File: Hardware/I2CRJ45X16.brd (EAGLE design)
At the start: 146 x 50 mm, 91 parts, among them IC1 MCP23017SO, IC2 MCP23017SO, IC3 MCP23017SO, IC4 MCP23017SO, J1 I2C-BREAKOUT, J2 I2C-BREAKOUT, J3 M01-PLAIN, J4 RJ45-X8, J5 RJ45-X8

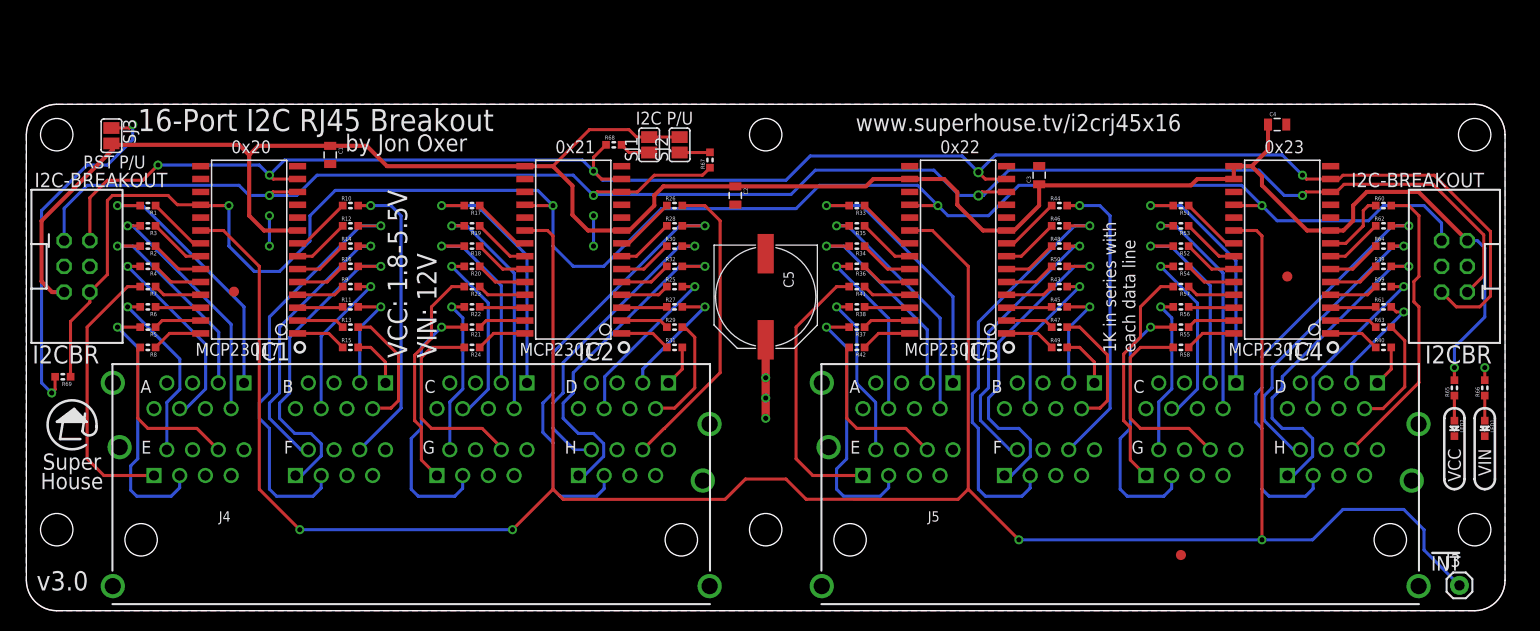
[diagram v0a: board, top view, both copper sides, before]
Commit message: Regenerated 16-port version from updated 24-port version.
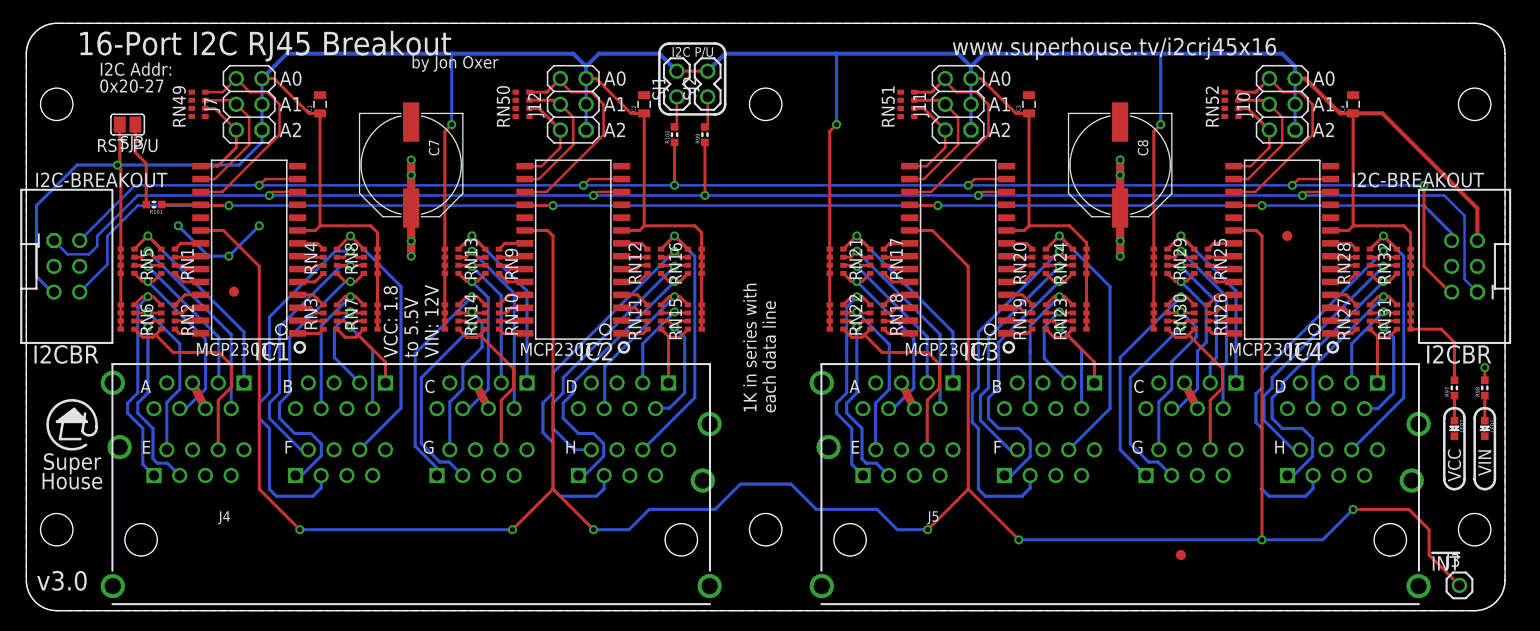
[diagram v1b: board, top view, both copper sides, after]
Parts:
- removed C5: 330uF 50V, SuperHouse-DiscreteSemi:PANASONIC_G
- removed R1, R10, R11, R12, R13, R14, R15, R16, R17, R18, R19, R2, R20, R21, R22, R23, R24, R25, R26, R27, R28, R29, R3, R30, R31, R32, R33, R34, R35, R36, R37, R38, R39, R4, R40, R41, R42, R43, R44, R45, R46, R47, R48, R49, R5, R50, R51, R52, R53, R54, R55, R56, R57, R58, R59, R6, R60, R61, R62, R63, R64, R7, R8, R9: 1K, SuperHouse-DiscreteSemi:R0603
- removed R65, R66, R67, R68: 4K7, SuperHouse-DiscreteSemi:R0603
- removed R69: 10K, SuperHouse-DiscreteSemi:R0603
- added C7, C8: 330uF 50V, SuperHouse-Capacitors:PANASONIC_G
- added J10: I2C Addr 4, SuperHouse-Connectors:2X03-P
- added J11: I2C Addr 3, SuperHouse-Connectors:2X03-P
- added J12: I2C Addr 2, SuperHouse-Connectors:2X03-P
- added J7: I2C Addr 1, SuperHouse-Connectors:2X03-P
- added R100, R97, R98, R99: 4K7, SuperHouse-Resistors:R0603
- added R101: 10K, SuperHouse-Resistors:R0603
- added RN1, RN10, RN11, RN12, RN17, RN18, RN19, RN2, RN20, RN25, RN26, RN27, RN28, RN3, RN4, RN9: 1K, SuperHouse-Resistors:CAY16
- added RN13, RN14, RN15, RN16, RN21, RN22, RN23, RN24, RN29, RN30, RN31, RN32, RN49, RN5, RN50, RN51, RN52, RN6, RN7, RN8: 10K, SuperHouse-Resistors:CAY16
- C1, C2, C3, C4: device SuperHouse-DiscreteSemi:C0805 -> SuperHouse-Capacitors:C0805
- J1, J2: device SuperHouse-Connectors:2X03-SHROUDED -> SuperHouse-Connectors:2X3-2.54-SHROUDED
- SJ1, SJ2: device SuperHouse-Jumpers:SJ -> SuperHouse-Connectors:1X02-P
- moved C2 12.7 mm to (61.0, 50.0), turned to 90 degrees
- moved C4 7.76 mm to (131.0, 50.0), turned to 90 degrees
- moved C3 7.07 mm to (99.0, 50.0)
- moved SJ2 6.61 mm to (67.3, 52.0)
- moved SJ1 6.59 mm to (64.2, 52.0)
- moved C1 5.10 mm to (29.0, 50.0), turned to 90 degrees
- moved FID2 4.00 mm to (124.5, 37.0)
- moved SJ3 1.94 mm to (10.0, 48.0), turned to 180 degrees
- moved J1 1.00 mm to (4.00, 34.0), turned to 270 degrees
- moved J2 1.00 mm to (142.0, 34.0), turned to 90 degrees
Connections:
- new net N$10: IC2.16, J12.4, RN50.7
- new net N$11: IC2.17, J12.6, RN50.8
- new net N$12: IC3.17, J11.6, RN51.8
- new net N$13: IC3.15, J11.2, RN51.6
- new net N$14: IC3.16, J11.4, RN51.7
- new net N$15: IC4.17, J10.6, RN52.8
- new net N$16: IC4.15, J10.2, RN52.6
- new net N$17: IC4.16, J10.4, RN52.7
- new net N$4: IC1.17, J7.6, RN49.8
- new net N$5: IC1.16, J7.4, RN49.7
- new net N$6: IC1.15, J7.2, RN49.6
- new net N$9: IC2.15, J12.2, RN50.6
- net !RESET: now also R101.1; no longer R69.1
- net 1A1: now also RN1.5, RN5.4; no longer R1.2
- net 1A2: now also RN1.6, RN5.3; no longer R3.2
- net 1A3: now also RN1.7, RN5.2; no longer R2.2
- net 1A6: now also RN1.8, RN5.1; no longer R4.2
- net 1B1: now also RN3.5, RN7.4; no longer R15.2
- net 1B2: now also RN3.6, RN7.3; no longer R13.2
- net 1B3: now also RN3.7, RN7.2; no longer R11.2
- net 1B6: now also RN3.8, RN7.1; no longer R9.2
- net 1C1: now also RN13.4, RN9.5; no longer R17.2
- net 1C2: now also RN13.3, RN9.6; no longer R19.2
- net 1C3: now also RN13.2, RN9.7; no longer R18.2
- net 1C6: now also RN13.1, RN9.8; no longer R20.2
- net 1D1: now also RN11.5, RN15.4; no longer R31.2
- net 1D2: now also RN11.6, RN15.3; no longer R29.2
- net 1D3: now also RN11.7, RN15.2; no longer R27.2
- net 1D6: now also RN11.8, RN15.1; no longer R25.2
- net 1E1: now also RN2.5, RN6.4; no longer R7.2
- net 1E2: now also RN2.6, RN6.3; no longer R6.2
- net 1E3: now also RN2.7, RN6.2; no longer R5.2
- net 1E6: now also RN2.8, RN6.1; no longer R8.2
- net 1F1: now also RN4.5, RN8.4; no longer R16.2
- net 1F2: now also RN4.6, RN8.3; no longer R14.2
- net 1F3: now also RN4.7, RN8.2; no longer R12.2
- net 1F6: now also RN4.8, RN8.1; no longer R10.2
- net 1G1: now also RN10.5, RN14.4; no longer R23.2
- net 1G2: now also RN10.6, RN14.3; no longer R22.2
- net 1G3: now also RN10.7, RN14.2; no longer R21.2
- net 1G6: now also RN10.8, RN14.1; no longer R24.2
- net 1H1: now also RN12.5, RN16.4; no longer R32.2
- net 1H2: now also RN12.6, RN16.3; no longer R30.2
- net 1H3: now also RN12.7, RN16.2; no longer R28.2
- net 1H6: now also RN12.8, RN16.1; no longer R26.2
- net 2A1: now also RN17.5, RN21.4; no longer R33.2
- net 2A2: now also RN17.6, RN21.3; no longer R35.2
- net 2A3: now also RN17.7, RN21.2; no longer R34.2
- net 2A6: now also RN17.8, RN21.1; no longer R36.2
- net 2B1: now also RN19.5, RN23.4; no longer R49.2
- net 2B2: now also RN19.6, RN23.3; no longer R47.2
- net 2B3: now also RN19.7, RN23.2; no longer R45.2
- net 2B6: now also RN19.8, RN23.1; no longer R43.2
- net 2C1: now also RN25.5, RN29.4; no longer R51.2
- net 2C2: now also RN25.6, RN29.3; no longer R53.2
- net 2C3: now also RN25.7, RN29.2; no longer R52.2
- net 2C6: now also RN25.8, RN29.1; no longer R54.2
- net 2D1: now also RN27.5, RN31.4; no longer R40.2
- net 2D2: now also RN27.6, RN31.3; no longer R63.2
- net 2D3: now also RN27.7, RN31.2; no longer R61.2
- net 2D6: now also RN27.8, RN31.1; no longer R59.2
- net 2E1: now also RN18.5, RN22.4; no longer R41.2
- net 2E2: now also RN18.6, RN22.3; no longer R38.2
- net 2E3: now also RN18.7, RN22.2; no longer R37.2
- net 2E6: now also RN18.8, RN22.1; no longer R42.2
- net 2F1: now also RN20.5, RN24.4; no longer R50.2
- net 2F2: now also RN20.6, RN24.3; no longer R48.2
- net 2F3: now also RN20.7, RN24.2; no longer R46.2
- net 2F6: now also RN20.8, RN24.1; no longer R44.2
- net 2G1: now also RN26.5, RN30.4; no longer R57.2
- net 2G2: now also RN26.6, RN30.3; no longer R56.2
- net 2G3: now also RN26.7, RN30.2; no longer R55.2
- net 2G6: now also RN26.8, RN30.1; no longer R58.2
- net 2H1: now also RN28.5, RN32.4; no longer R39.2
- net 2H2: now also RN28.6, RN32.3; no longer R64.2
- net 2H3: now also RN28.7, RN32.2; no longer R62.2
- net 2H6: now also RN28.8, RN32.1; no longer R60.2
- net GND: now also C7.-, C8.-, RN49.1, RN49.2, RN49.3, RN49.4, RN50.1, RN50.2, RN50.3, RN50.4, RN51.1, RN51.2, RN51.3, RN51.4, RN52.1, RN52.2, RN52.3, RN52.4; no longer C5.-, IC1.15, IC1.16, IC1.17, IC2.16, IC2.17, IC3.15, IC3.17, IC4.17
- net GPA0-1: now also RN1.4; no longer R1.1
- net GPA0-2: now also RN9.4; no longer R17.1
- net GPA0-3: now also RN17.4; no longer R33.1
- net GPA0-4: now also RN25.4; no longer R51.1
- net GPA1-1: now also RN1.3; no longer R3.1
- net GPA1-2: now also RN9.3; no longer R19.1
- net GPA1-3: now also RN17.3; no longer R35.1
- net GPA1-4: now also RN25.3; no longer R53.1
- net GPA2-1: now also RN1.2; no longer R2.1
- net GPA2-2: now also RN9.2; no longer R18.1
- net GPA2-3: now also RN17.2; no longer R34.1
- net GPA2-4: now also RN25.2; no longer R52.1
- net GPA3-1: now also RN1.1; no longer R4.1
- net GPA3-2: now also RN9.1; no longer R20.1
- net GPA3-3: now also RN17.1; no longer R36.1
- net GPA3-4: now also RN25.1; no longer R54.1
- net GPA4-1: now also RN2.4; no longer R7.1
- net GPA4-2: now also RN10.4; no longer R23.1
- net GPA4-3: now also RN18.4; no longer R41.1
- net GPA4-4: now also RN26.4; no longer R57.1
- net GPA5-1: now also RN2.3; no longer R6.1
- net GPA5-2: now also RN10.3; no longer R22.1
- net GPA5-3: now also RN18.3; no longer R38.1
- net GPA5-4: now also RN26.3; no longer R56.1
- net GPA6-1: now also RN2.2; no longer R5.1
- net GPA6-2: now also RN10.2; no longer R21.1
- net GPA6-3: now also RN18.2; no longer R37.1
- net GPA6-4: now also RN26.2; no longer R55.1
- net GPA7-1: now also RN2.1; no longer R8.1
- net GPA7-2: now also RN10.1; no longer R24.1
- net GPA7-3: now also RN18.1; no longer R42.1
- net GPA7-4: now also RN26.1; no longer R58.1
- net GPB0-1: now also RN3.4; no longer R15.1
- net GPB0-2: now also RN11.4; no longer R31.1
- net GPB0-3: now also RN19.4; no longer R49.1
- net GPB0-4: now also RN27.4; no longer R40.1
- net GPB1-1: now also RN3.3; no longer R13.1
- net GPB1-2: now also RN11.3; no longer R29.1
- net GPB1-3: now also RN19.3; no longer R47.1
- net GPB1-4: now also RN27.3; no longer R63.1
- net GPB2-1: now also RN3.2; no longer R11.1
- net GPB2-2: now also RN11.2; no longer R27.1
- net GPB2-3: now also RN19.2; no longer R45.1
- net GPB2-4: now also RN27.2; no longer R61.1
- net GPB3-1: now also RN3.1; no longer R9.1
- net GPB3-2: now also RN11.1; no longer R25.1
- net GPB3-3: now also RN19.1; no longer R43.1
- net GPB3-4: now also RN27.1; no longer R59.1
- net GPB4-1: now also RN4.4; no longer R16.1
- net GPB4-2: now also RN12.4; no longer R32.1
- net GPB4-3: now also RN20.4; no longer R50.1
- net GPB4-4: now also RN28.4; no longer R39.1
- net GPB5-1: now also RN4.3; no longer R14.1
- net GPB5-2: now also RN12.3; no longer R30.1
- net GPB5-3: now also RN20.3; no longer R48.1
- net GPB5-4: now also RN28.3; no longer R64.1
- net GPB6-1: now also RN4.2; no longer R12.1
- net GPB6-2: now also RN12.2; no longer R28.1
- net GPB6-3: now also RN20.2; no longer R46.1
- net GPB6-4: now also RN28.2; no longer R62.1
- net GPB7-1: now also RN4.1; no longer R10.1
- net GPB7-2: now also RN12.1; no longer R26.1
- net GPB7-3: now also RN20.1; no longer R44.1
- net GPB7-4: now also RN28.1; no longer R60.1
- net N$1: now also R99.2; no longer R67.2
- net N$2: now also R100.2; no longer R68.2
- net N$3: now also R101.2; no longer R69.2
- net N$7: now also R97.1; no longer R65.1
- net N$8: now also R98.1; no longer R66.1
- net SCL: now also R99.1; no longer R67.1
- net SDA: now also R100.1; no longer R68.1
- net VCC: now also J10.1, J10.3, J10.5, J11.1, J11.3, J11.5, J12.1, J12.3, J12.5, J7.1, J7.3, J7.5, R97.2, RN13.5, RN13.6, RN13.7, RN13.8, RN14.5, RN14.6, RN14.7, RN14.8, RN15.5, RN15.6, RN15.7, RN15.8, RN16.5, RN16.6, RN16.7, RN16.8, RN21.5, RN21.6, RN21.7, RN21.8, RN22.5, RN22.6, RN22.7, RN22.8, RN23.5, RN23.6, RN23.7, RN23.8, RN24.5, RN24.6, RN24.7, RN24.8, RN29.5, RN29.6, RN29.7, RN29.8, RN30.5, RN30.6, RN30.7, RN30.8, RN31.5, RN31.6, RN31.7, RN31.8, RN32.5, RN32.6, RN32.7, RN32.8, RN5.5, RN5.6, RN5.7, RN5.8, RN6.5, RN6.6, RN6.7, RN6.8, RN7.5, RN7.6, RN7.7, RN7.8, RN8.5, RN8.6, RN8.7, RN8.8; no longer IC2.15, IC3.16, IC4.15, IC4.16, R65.2
- net VIN: now also C7.+, C8.+, R98.2; no longer C5.+, R66.2
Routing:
- net VCC: track 223.5 -> 441.2 mm, vias 1 -> 4
- net !RESET: track 185.3 -> 157.6 mm
- net N$3: track 35.8 -> 8.35 mm, vias 2 -> 0
- net VIN: track 8.99 -> 31.6 mm, vias 4 -> 9
- net N$12: track 0.00 -> 22.1 mm
- net N$11: track 0.00 -> 22.1 mm
- net N$4: track 0.00 -> 22.1 mm
- net N$15: track 0.00 -> 22.0 mm
- net N$17: track 0.00 -> 13.9 mm
- net N$14: track 0.00 -> 13.9 mm
- net N$10: track 0.00 -> 13.9 mm
- net N$5: track 0.00 -> 13.9 mm
- net N$16: track 0.00 -> 9.94 mm
- net N$13: track 0.00 -> 9.94 mm
- net N$9: track 0.00 -> 9.94 mm
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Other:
- board size 146 x 50 mm -> 146 x 58 mm
- board text added: "A0"
- board text added: "A1"
- board text added: "A2"
- board text added: "I2C Addr: 0x20-27"
- board text added: "VCC: 1.8 to 5.5V VIN: 12V"
- board text removed: "0x20"
- board text removed: "0x21"
- board text removed: "0x22"
- board text removed: "0x23"
- board text removed: "VCC: 1.8-5.5V VIN: 12V"
